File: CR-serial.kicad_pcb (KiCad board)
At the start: 2 copper layers, 55.6 x 40.6 mm, 26 parts, among them J1 USB, J2 GPIO, J3 UART0, J4 UART1, J5 UART2, J6 UART3_HV, J7 RS232_0, J8 RS232_1, U1 CP2108-xxx-xM, U2 MAX232

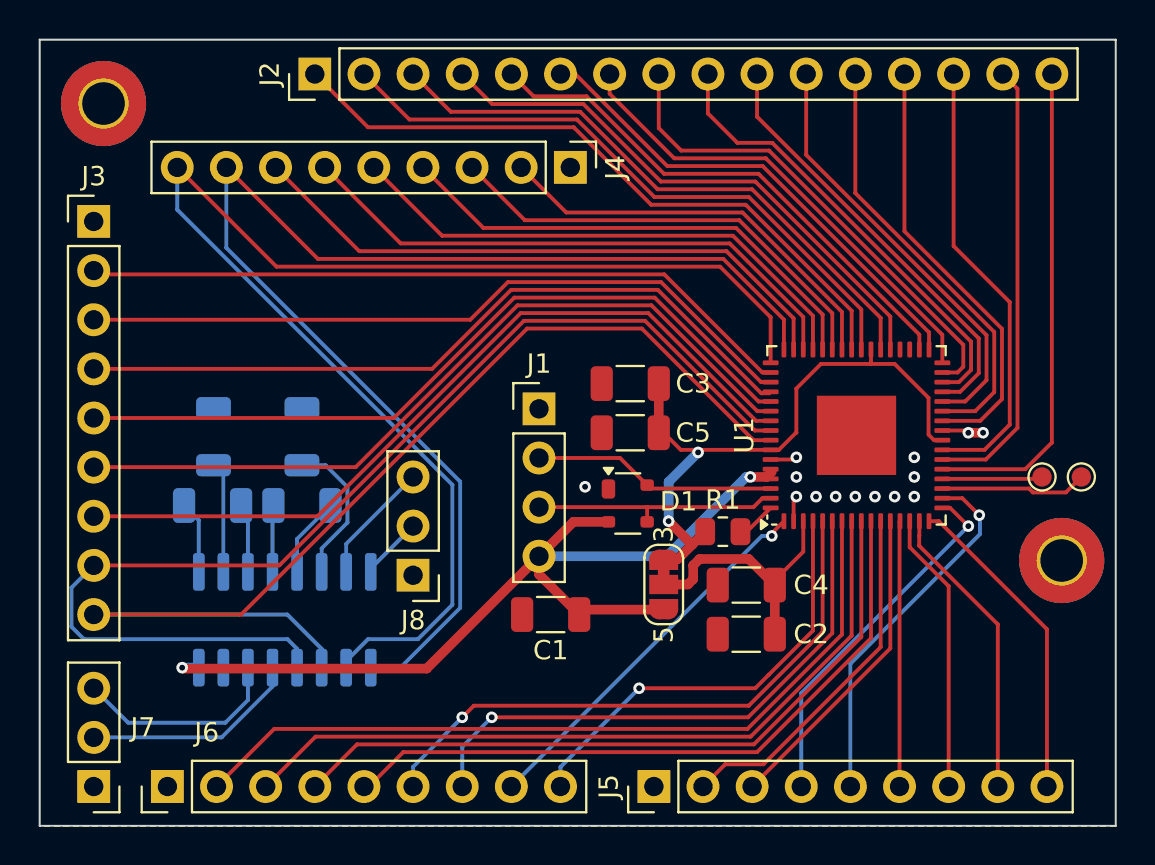
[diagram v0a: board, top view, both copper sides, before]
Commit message: Make GPIO header double-row
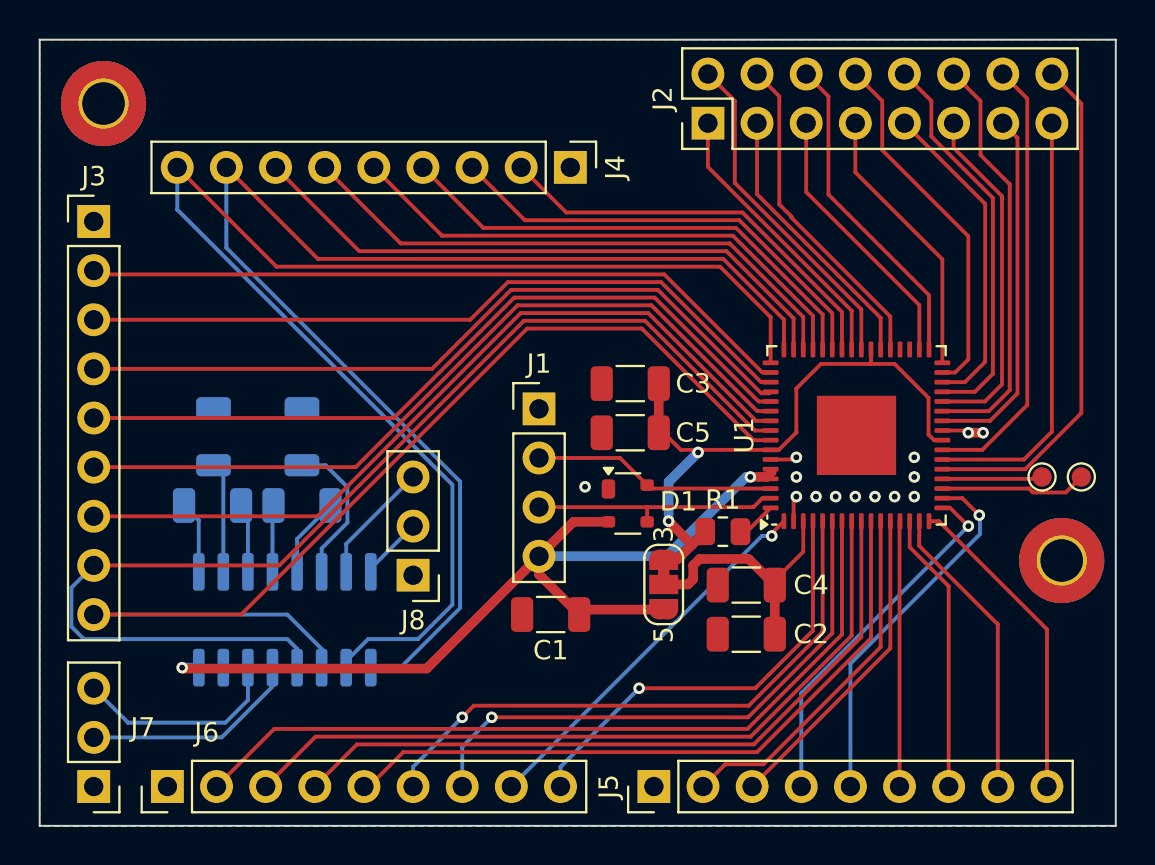
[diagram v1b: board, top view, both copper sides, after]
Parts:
- J2: footprint Connector_PinHeader_2.54mm:PinHeader_1x16_P2.54mm_Vertical -> Connector_PinHeader_2.54mm:PinHeader_2x08_P2.54mm_Vertical
- moved J2 20.5 mm to (192.3, 100.8)
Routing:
- net Net-(J2-Pin_1): track 34.8 -> 14.8 mm
- net Net-(J2-Pin_3): track 31.0 -> 14.3 mm
- net Net-(J2-Pin_2): track 32.8 -> 17.5 mm
- net Net-(J2-Pin_5): track 27.4 -> 14.1 mm
- net Net-(J2-Pin_4): track 29.0 -> 17.1 mm
- net Net-(J2-Pin_7): track 24.8 -> 14.2 mm
- net Net-(J2-Pin_6): track 25.5 -> 16.9 mm
- net Net-(J2-Pin_9): track 23.7 -> 16.7 mm
- net Net-(J2-Pin_8): track 25.5 -> 18.8 mm
- net Net-(J2-Pin_11): track 22.4 -> 18.0 mm
- net Net-(J2-Pin_13): track 22.4 -> 18.8 mm
- net Net-(J2-Pin_10): track 22.5 -> 20.4 mm
- net Net-(J2-Pin_16): track 25.3 -> 26.5 mm
- net Net-(J2-Pin_12): track 22.5 -> 21.5 mm
- net Net-(J2-Pin_15): track 23.2 -> 22.2 mm

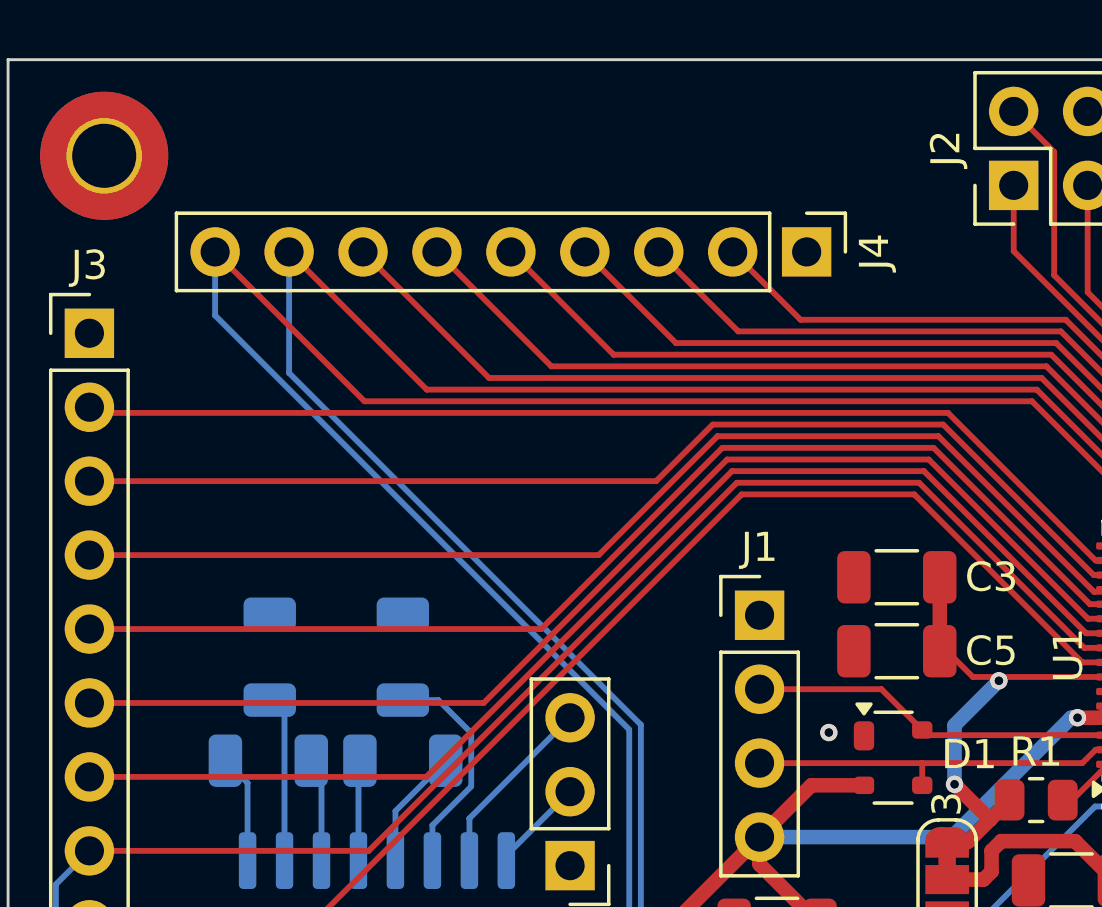
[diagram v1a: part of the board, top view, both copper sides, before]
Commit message: Move UART1 header to the edge of the board
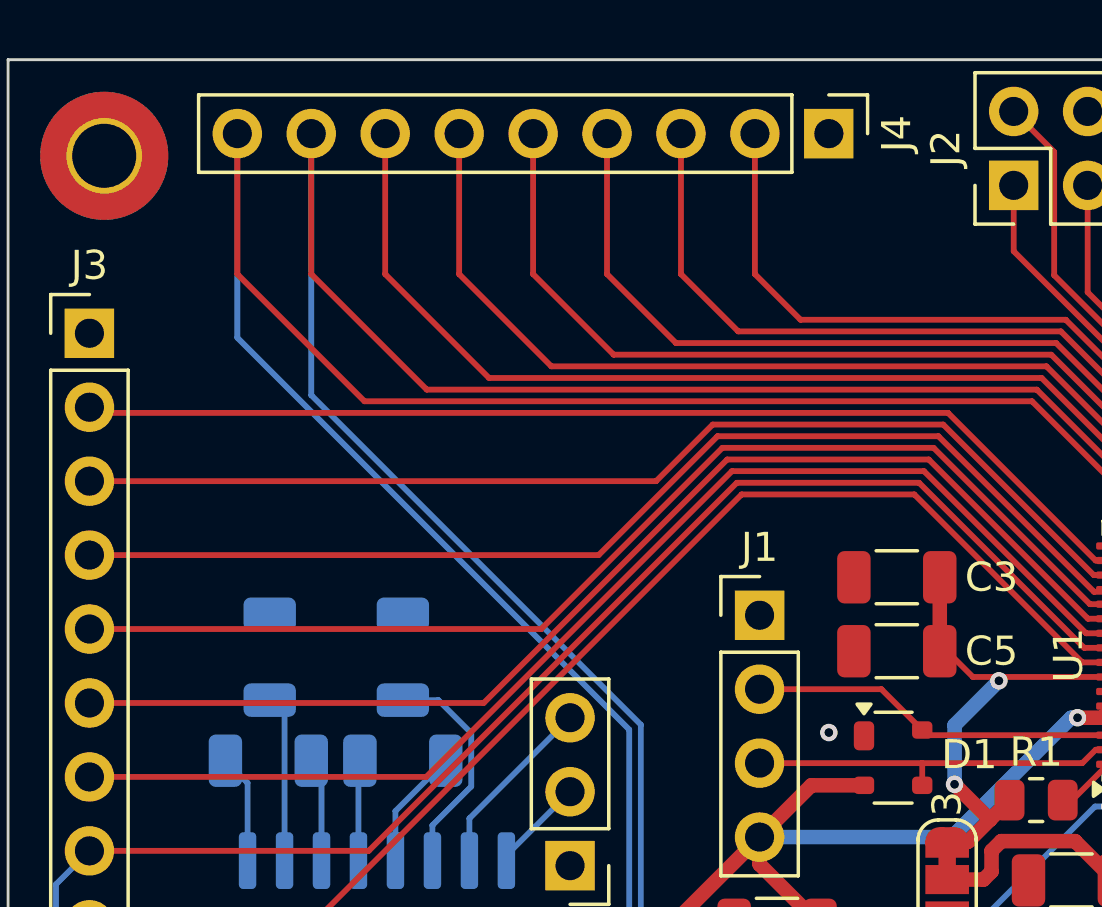
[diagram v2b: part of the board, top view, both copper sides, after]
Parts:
- moved J4 4.13 mm to (185.9, 99.1)
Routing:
- net /TX1: track 71.8 -> 79.3 mm
- net /RX1: track 67.3 -> 74.8 mm
- net Net-(J4-Pin_7): track 31.6 -> 35.4 mm
- net Net-(J4-Pin_6): track 29.6 -> 33.4 mm
- net Net-(J4-Pin_5): track 27.6 -> 31.4 mm
- net Net-(J4-Pin_4): track 25.6 -> 29.4 mm
- net Net-(J4-Pin_3): track 23.6 -> 27.4 mm
- net Net-(J4-Pin_2): track 21.6 -> 25.4 mm
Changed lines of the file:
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@@
 	(footprint "Connector_PinHeader_2.54mm:PinHeader_1x09_P2.54mm_Vertical"
 		(layer "F.Cu")
-		(at 185.166 103.124 -90)
+		(at 185.928 99.06 -90)
 		(descr "Through hole straight pin header, 1x09, 2.54mm pitch, single row")
 		(tags "Through hole pin header THT 1x09 2.54mm single row")
@@
 	)
 	(segment
-		(start 195.5205 110.868732)
-		(end 195.5205 113.2245)
+		(start 169.976 108.254)
+		(end 192.905768 108.254)
 		(width 0.2)
 		(layer "F.Cu")
@@
 	)
 	(segment
-		(start 169.976 108.254)
-		(end 192.905768 108.254)
+		(start 165.608 103.886)
+		(end 169.976 108.254)
 		(width 0.2)
 		(layer "F.Cu")
@@
 	)
 	(segment
-		(start 164.846 103.124)
-		(end 169.976 108.254)
+		(start 165.608 99.06)
+		(end 165.608 103.886)
+		(width 0.2)
+		(layer "F.Cu")
+		(net 37)
+	)
+	(segment
+		(start 195.5205 110.868732)
+		(end 195.5205 113.2245)
 		(width 0.2)
 		(layer "F.Cu")
@@
 	)
 	(segment
-		(start 177.292 127.508)
-		(end 179.07 125.73)
+		(start 179.07 119.531654)
+		(end 165.608 106.069654)
 		(width 0.2)
 		(layer "B.Cu")
@@
 	)
 	(segment
-		(start 179.07 119.531654)
-		(end 164.846 105.307654)
+		(start 165.608 106.069654)
+		(end 165.608 99.06)
 		(width 0.2)
 		(layer "B.Cu")
@@
 	)
 	(segment
-		(start 164.846 105.307654)
-		(end 164.846 103.124)
+		(start 174.709448 127.508)
+		(end 177.292 127.508)
 		(width 0.2)
 		(layer "B.Cu")
@@
 	)
 	(segment
-		(start 174.709448 127.508)
-		(end 177.292 127.508)
+		(start 173.58 128.983)
+		(end 173.58 128.637448)
 		(width 0.2)
 		(layer "B.Cu")
@@
 	)
 	(segment
-		(start 173.58 128.983)
-		(end 173.58 128.637448)
+		(start 177.292 127.508)
+		(end 179.07 125.73)
 		(width 0.2)
 		(layer "B.Cu")
@@
 	)
 	(segment
+		(start 180.848 103.886)
+		(end 182.816 105.854)
+		(width 0.2)
+		(layer "F.Cu")
+		(net 38)
+	)
+	(segment
+		(start 198.708 110.662116)
+		(end 198.708 112.537)
+		(width 0.2)
+		(layer "F.Cu")
+		(net 38)
+	)
+	(segment
 		(start 193.899884 105.854)
 		(end 198.708 110.662116)
@@
 	)
 	(segment
-		(start 182.816 105.854)
-		(end 193.899884 105.854)
+		(start 180.848 99.06)
+		(end 180.848 103.886)
 		(width 0.2)
 		(layer "F.Cu")
@@
 	)
 	(segment
-		(start 198.708 110.662116)
-		(end 198.708 112.537)
+		(start 182.816 105.854)
+		(end 193.899884 105.854)
 		(width 0.2)
 		(layer "F.Cu")
@@
 	)
 	(segment
-		(start 180.086 103.124)
-		(end 182.816 105.854)
+		(start 199.208 110.59643)
+		(end 199.208 112.537)
 		(width 0.2)
 		(layer "F.Cu")
-		(net 38)
+		(net 39)
 	)
 	(segment
@@
 	)
 	(segment
-		(start 199.208 110.59643)
-		(end 199.208 112.537)
+		(start 183.388 99.06)
+		(end 183.388 103.886)
 		(width 0.2)
 		(layer "F.Cu")
@@
 	)
 	(segment
-		(start 182.626 103.124)
+		(start 183.388 103.886)
 		(end 184.956 105.454)
 		(width 0.2)
@@
 	)
 	(segment
-		(start 167.386 103.124)
-		(end 172.116 107.854)
+		(start 172.116 107.854)
+		(end 193.071454 107.854)
 		(width 0.2)
 		(layer "F.Cu")
@@
 	)
 	(segment
-		(start 193.071454 107.854)
-		(end 196.208 110.990546)
+		(start 196.208 110.990546)
+		(end 196.208 112.537)
 		(width 0.2)
 		(layer "F.Cu")
@@
 	)
 	(segment
-		(start 196.208 110.990546)
-		(end 196.208 112.537)
+		(start 168.148 103.886)
+		(end 172.116 107.854)
 		(width 0.2)
 		(layer "F.Cu")
@@
 	)
 	(segment
-		(start 172.116 107.854)
-		(end 193.071454 107.854)
+		(start 168.148 99.06)
+		(end 168.148 103.886)
 		(width 0.2)
 		(layer "F.Cu")
@@
 	)
 	(segment
-		(start 179.47 125.895686)
-		(end 179.47 119.365968)
+		(start 193.071454 107.854)
+		(end 196.208 110.990546)
+		(width 0.2)
+		(layer "F.Cu")
+		(net 40)
+	)
+	(segment
+		(start 176.382686 128.983)
+		(end 179.47 125.895686)
 		(width 0.2)
 		(layer "B.Cu")
@@
 	)
 	(segment
-		(start 179.47 119.365968)
-		(end 167.386 107.281968)
+		(start 179.47 125.895686)
+		(end 179.47 119.365968)
 		(width 0.2)
 		(layer "B.Cu")
@@
 	)
 	(segment
-		(start 174.85 128.983)
-		(end 176.382686 128.983)
+		(start 168.148 108.043968)
+		(end 168.148 99.06)
 		(width 0.2)
 		(layer "B.Cu")
@@
 	)
 	(segment
-		(start 167.386 107.281968)
-		(end 167.386 103.124)
+		(start 179.47 119.365968)
+		(end 168.148 108.043968)
 		(width 0.2)
 		(layer "B.Cu")
@@
 	)
 	(segment
-		(start 176.382686 128.983)
-		(end 179.47 125.895686)
+		(start 174.85 128.983)
+		(end 176.382686 128.983)
 		(width 0.2)
 		(layer "B.Cu")
@@
 	)
 	(segment
-		(start 177.546 103.124)
+		(start 178.308 103.886)
 		(end 180.676 106.254)
 		(width 0.2)
@@
 	)
 	(segment
+		(start 178.308 99.06)
+		(end 178.308 103.886)
+		(width 0.2)
+		(layer "F.Cu")
+		(net 41)
+	)
+	(segment
 		(start 180.676 106.254)
 		(end 193.734198 106.254)
@@
 	)
 	(segment
-		(start 193.568512 106.654)
-		(end 197.708 110.793488)
+		(start 175.768 103.886)
+		(end 178.536 106.654)
 		(width 0.2)
 		(layer "F.Cu")
@@
 	)
 	(segment
-		(start 178.536 106.654)
-		(end 193.568512 106.654)
+		(start 175.768 99.06)
+		(end 175.768 103.886)
+		(width 0.2)
+		(layer "F.Cu")
+		(net 42)
+	)
+	(segment
+		(start 193.568512 106.654)
+		(end 197.708 110.793488)
 		(width 0.2)
 		(layer "F.Cu")
@@
 	)
 	(segment
-		(start 175.006 103.124)
-		(end 178.536 106.654)
+		(start 178.536 106.654)
+		(end 193.568512 106.654)
 		(width 0.2)
 		(layer "F.Cu")
@@
 	)
 	(segment
-		(start 172.466 103.124)
-		(end 176.396 107.054)
+		(start 173.228 99.06)
+		(end 173.228 103.886)
 		(width 0.2)
 		(layer "F.Cu")
@@
 	)
 	(segment
-		(start 193.402826 107.054)
-		(end 197.208 110.859174)
+		(start 176.396 107.054)
+		(end 193.402826 107.054)
 		(width 0.2)
 		(layer "F.Cu")
@@
 	)
 	(segment
-		(start 176.396 107.054)
-		(end 193.402826 107.054)
+		(start 173.228 103.886)
+		(end 176.396 107.054)
 		(width 0.2)
 		(layer "F.Cu")
@@
 	)
 	(segment
-		(start 169.926 103.124)
-		(end 174.256 107.454)
+		(start 193.402826 107.054)
+		(end 197.208 110.859174)
 		(width 0.2)
 		(layer "F.Cu")
-		(net 44)
+		(net 43)
 	)
 	(segment
@@
 	)
 	(segment
+		(start 170.688 99.06)
+		(end 170.688 103.886)
+		(width 0.2)
+		(layer "F.Cu")
+		(net 44)
+	)
+	(segment
 		(start 196.708 110.92486)
 		(end 196.708 112.537)
@@
 		(width 0.2)
 		(layer "F.Cu")
+		(net 44)
+	)
+	(segment
+		(start 170.688 103.886)
+		(end 174.256 107.454)
+		(width 0.2)
+		(layer "F.Cu")
